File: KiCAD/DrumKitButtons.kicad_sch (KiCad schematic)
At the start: 6 parts, among them J1 Input, J2 Output

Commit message: fix DRC errors
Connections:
- net DI_{LED}: now also J2.4 (Pin_4); no longer J1.4 (Pin_4)
- net DI_{SW}: now also J1.5 (Pin_5); no longer J2.5 (Pin_5)
- net DO_{LED}: now also J1.4 (Pin_4); no longer J2.4 (Pin_4)
- net DO_{SW}: now also J2.5 (Pin_5); no longer J1.5 (Pin_5)
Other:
- moved on the sheet: J1

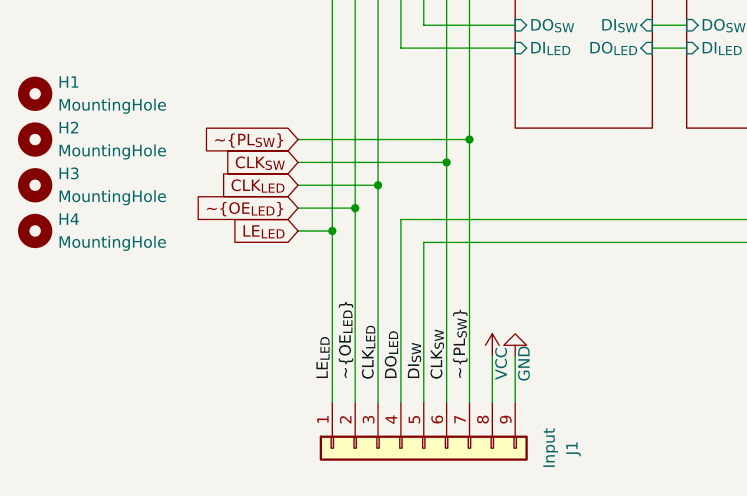
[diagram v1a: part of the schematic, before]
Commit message: reorder buttons/leds
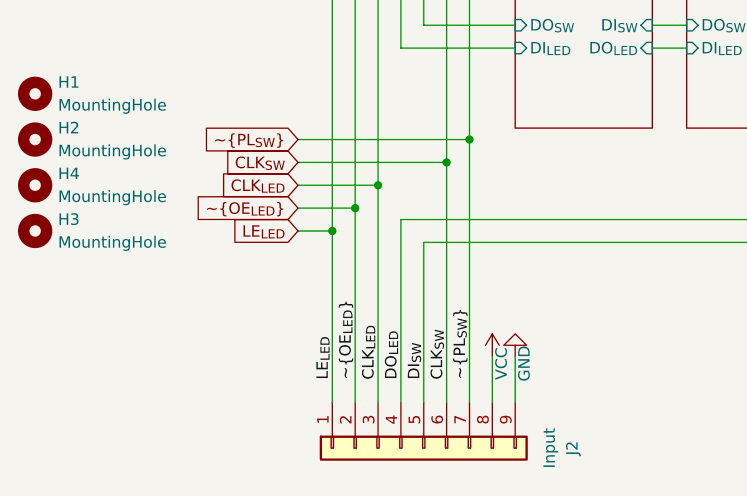
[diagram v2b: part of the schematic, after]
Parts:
- renumbered H4 to H3, H3 to H4, J2 to J1, J1 to J2
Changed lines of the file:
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@@
 		(dnp no)
 		(fields_autoplaced yes)
-		(property "Reference" "J2"
+		(property "Reference" "J1"
 			(at 109.22 46.99 0)
 			(effects
@@
 			(project "DrumKitButtons"
 				(path "/9053e4fd-2214-4e2c-a1c2-d5a9964413b7"
-					(reference "J2")
+					(reference "J1")
 					(unit 1)
 				)
@@
 		(on_board yes)
 		(dnp no)
-		(property "Reference" "#PWR023"
+		(property "Reference" "#PWR04"
 			(at 101.6 119.38 0)
 			(effects
@@
 			(project "DrumKitButtons"
 				(path "/9053e4fd-2214-4e2c-a1c2-d5a9964413b7"
-					(reference "#PWR023")
+					(reference "#PWR04")
 					(unit 1)
 				)
@@
 		(dnp no)
 		(fields_autoplaced yes)
-		(property "Reference" "J1"
+		(property "Reference" "J2"
 			(at 107.95 135.89 0)
 			(effects
@@
 			(project ""
 				(path "/9053e4fd-2214-4e2c-a1c2-d5a9964413b7"
-					(reference "J1")
+					(reference "J2")
 					(unit 1)
 				)
@@
 		(on_board yes)
 		(dnp no)
-		(property "Reference" "#PWR024"
+		(property "Reference" "#PWR03"
 			(at 99.06 129.54 0)
 			(effects
@@
 			(project "DrumKitButtons"
 				(path "/9053e4fd-2214-4e2c-a1c2-d5a9964413b7"
-					(reference "#PWR024")
+					(reference "#PWR03")
 					(unit 1)
 				)
@@
 		(on_board yes)
 		(dnp no)
-		(property "Reference" "#PWR021"
+		(property "Reference" "#PWR01"
 			(at 99.06 55.88 0)
 			(effects
@@
 			(project "DrumKitButtons"
 				(path "/9053e4fd-2214-4e2c-a1c2-d5a9964413b7"
-					(reference "#PWR021")
+					(reference "#PWR01")
 					(unit 1)
 				)
@@
 		(dnp no)
 		(fields_autoplaced yes)
-		(property "Reference" "H4"
+		(property "Reference" "H3"
 			(at 50.8 110.4899 0)
 			(effects
@@
 			(project ""
 				(path "/9053e4fd-2214-4e2c-a1c2-d5a9964413b7"
-					(reference "H4")
+					(reference "H3")
 					(unit 1)
 				)
@@
 		(dnp no)
 		(fields_autoplaced yes)
-		(property "Reference" "H3"
+		(property "Reference" "H4"
 			(at 50.8 105.4099 0)
 			(effects
@@
 			(project ""
 				(path "/9053e4fd-2214-4e2c-a1c2-d5a9964413b7"
-					(reference "H3")
+					(reference "H4")
 					(unit 1)
 				)
@@
 		(on_board yes)
 		(dnp no)
-		(property "Reference" "#PWR022"
+		(property "Reference" "#PWR02"
 			(at 101.6 66.04 0)
 			(effects
@@
 			(project "DrumKitButtons"
 				(path "/9053e4fd-2214-4e2c-a1c2-d5a9964413b7"
-					(reference "#PWR022")
-					(unit 1)
-				)
+					(reference "#PWR02")
+					(unit 1)
+				)

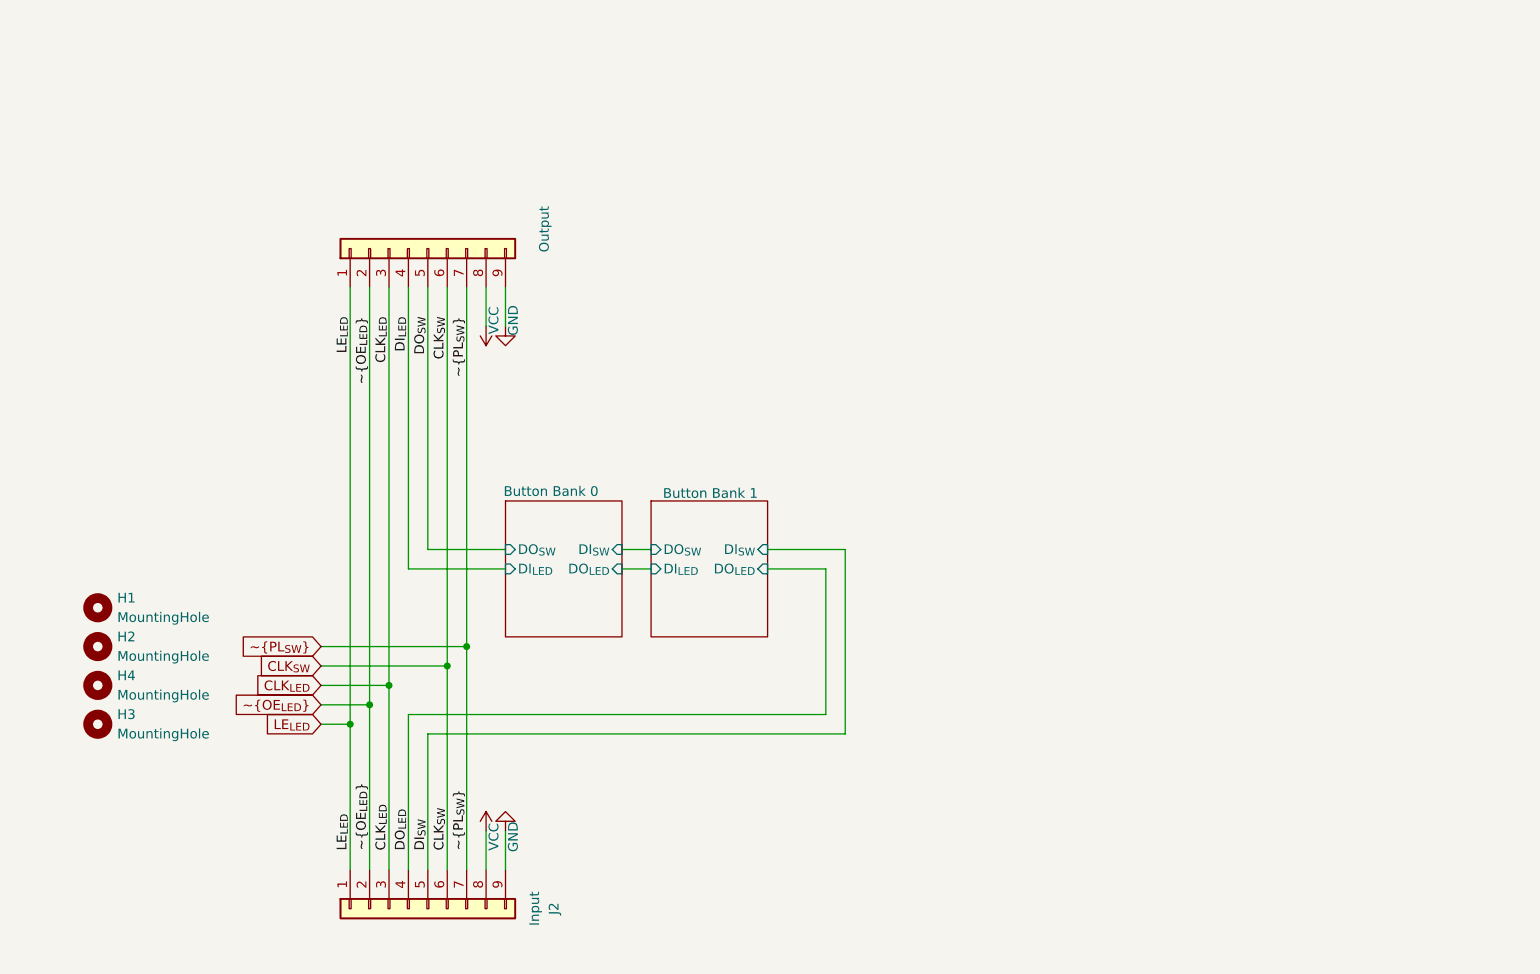
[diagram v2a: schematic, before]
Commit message: make 3 rows in schema; break single button out to its own kicad_sch
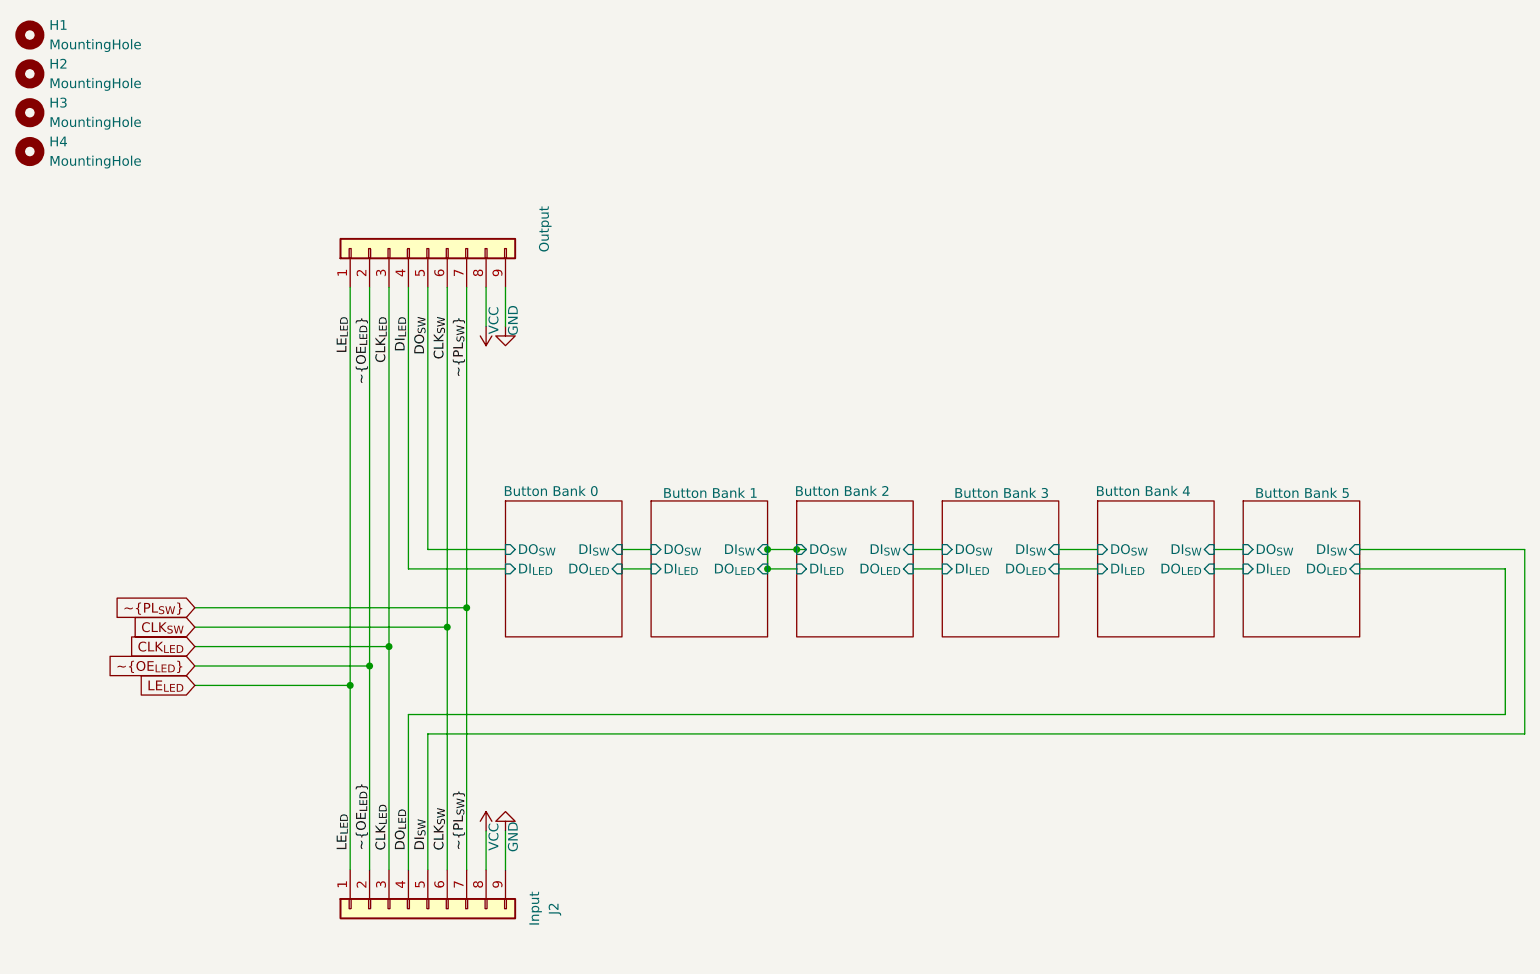
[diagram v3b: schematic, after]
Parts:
- renumbered H4 to H3, H3 to H4
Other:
- added sheet Button Bank 2 (8-buttons.kicad_sch)
- added sheet Button Bank 3 (8-buttons.kicad_sch)
- added sheet Button Bank 4 (8-buttons.kicad_sch)
- added sheet Button Bank 5 (8-buttons.kicad_sch)
- moved on the sheet: H1, H2, H3, H4

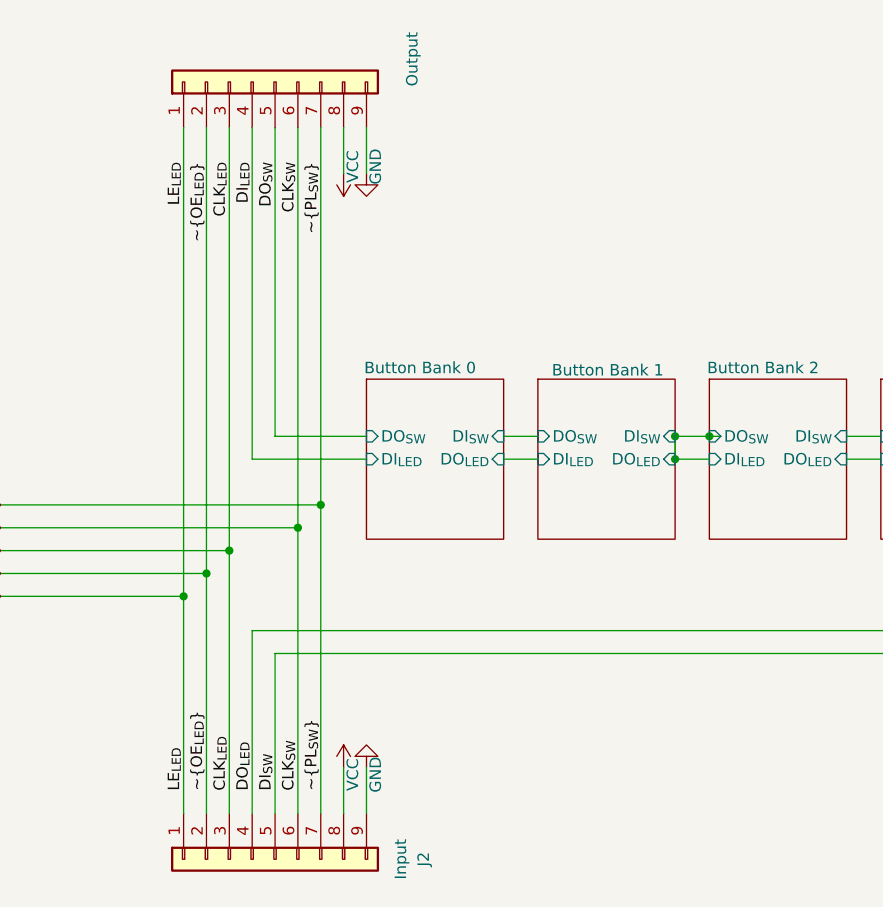
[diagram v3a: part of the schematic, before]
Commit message: 3 rows of 16 buttons; SMT
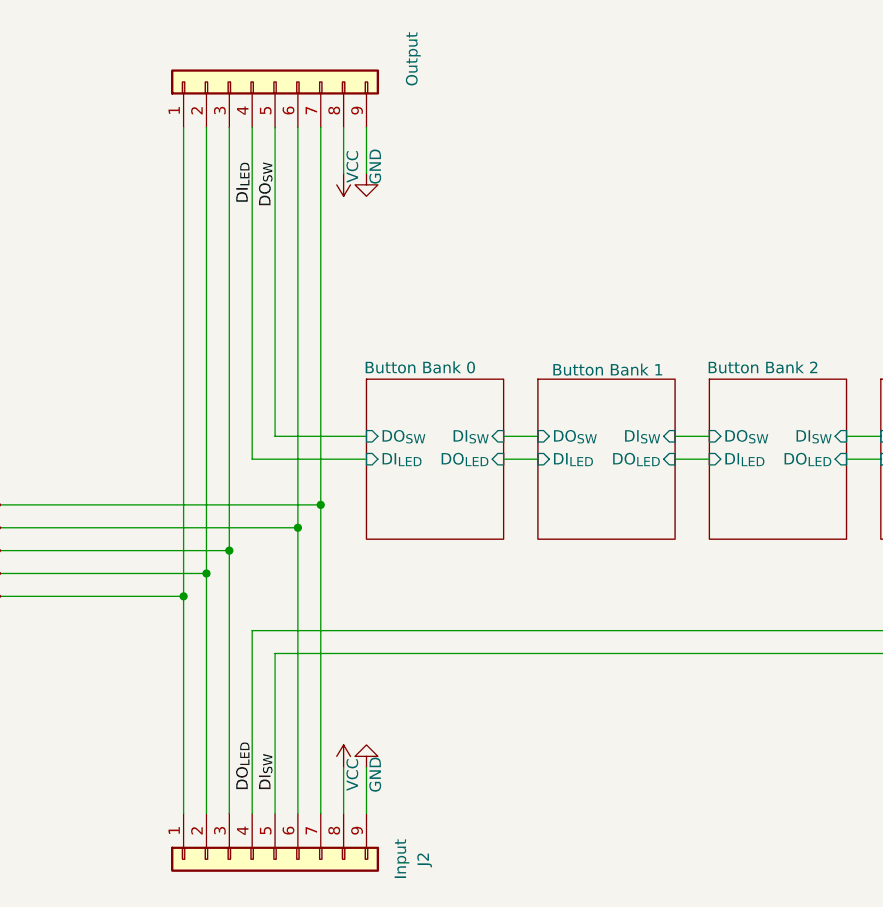
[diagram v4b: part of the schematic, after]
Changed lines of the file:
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@@
-	)
-	(junction
-		(at 135.89 88.9)
-		(diameter 0)
-		(color 0 0 0 0)
-	)
-	(junction
-		(at 139.7 88.9)
-		(diameter 0)
-		(color 0 0 0 0)
-	)
-	(junction
-		(at 135.89 91.44)
-		(diameter 0)
-		(color 0 0 0 0)
 	)
 	(junction
@@
 		(pts
 			(xy 86.36 54.61) (xy 86.36 101.6)
-		)
-		(stroke
-			(width 0)
-			(type default)
-		)
-	)
-	(wire
-		(pts
-			(xy 135.89 88.9) (xy 135.89 91.44)
-		)
-		(stroke
-			(width 0)
-			(type default)
-		)
-	)
-	(wire
-		(pts
-			(xy 139.7 88.9) (xy 140.97 88.9)
 		)
 		(stroke
@@
 		)
 	)
-	(label "LE_{LED}"
-		(at 81.28 128.27 90)
-		(effects
-			(font
-				(size 1.27 1.27)
-			)
-			(justify left bottom)
-		)
-	)
-	(label "~{OE_{LED}}"
-		(at 83.82 58.42 270)
-		(effects
-			(font
-				(size 1.27 1.27)
-			)
-			(justify right bottom)
-		)
-	)
-	(label "CLK_{SW}"
-		(at 93.98 58.42 270)
-		(effects
-			(font
-				(size 1.27 1.27)
-			)
-			(justify right bottom)
-		)
-	)
 	(label "DI_{LED}"
 		(at 88.9 58.42 270)
@@
 		(effects
 			(font
-				(size 1.27 1.27)
-			)
-			(justify left bottom)
-		)
-	)
-	(label "LE_{LED}"
-		(at 81.28 58.42 270)
-		(effects
-			(font
-				(size 1.27 1.27)
-			)
-			(justify right bottom)
-		)
-	)
-	(label "~{OE_{LED}}"
-		(at 83.82 128.27 90)
-		(effects
-			(font
-				(size 1.27 1.27)
-			)
-			(justify left bottom)
-		)
-	)
-	(label "CLK_{LED}"
-		(at 86.36 128.27 90)
-		(effects
-			(font
-				(size 1.27 1.27)
-			)
-			(justify left bottom)
-		)
-	)
-	(label "~{PL_{SW}}"
-		(at 96.52 128.27 90)
-		(effects
-			(font
-				(size 1.27 1.27)
-			)
-			(justify left bottom)
-		)
-	)
-	(label "CLK_{LED}"
-		(at 86.36 58.42 270)
-		(effects
-			(font
-				(size 1.27 1.27)
-			)
-			(justify right bottom)
-		)
-	)
-	(label "~{PL_{SW}}"
-		(at 96.52 58.42 270)
-		(effects
-			(font
-				(size 1.27 1.27)
-			)
-			(justify right bottom)
-		)
-	)
-	(label "CLK_{SW}"
-		(at 93.98 128.27 90)
-		(effects
-			(font

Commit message: Revert "3 rows of 16 buttons; SMT"
This reverts commit c08e4dc0c350e57a2ca7329c2459be699e742724.
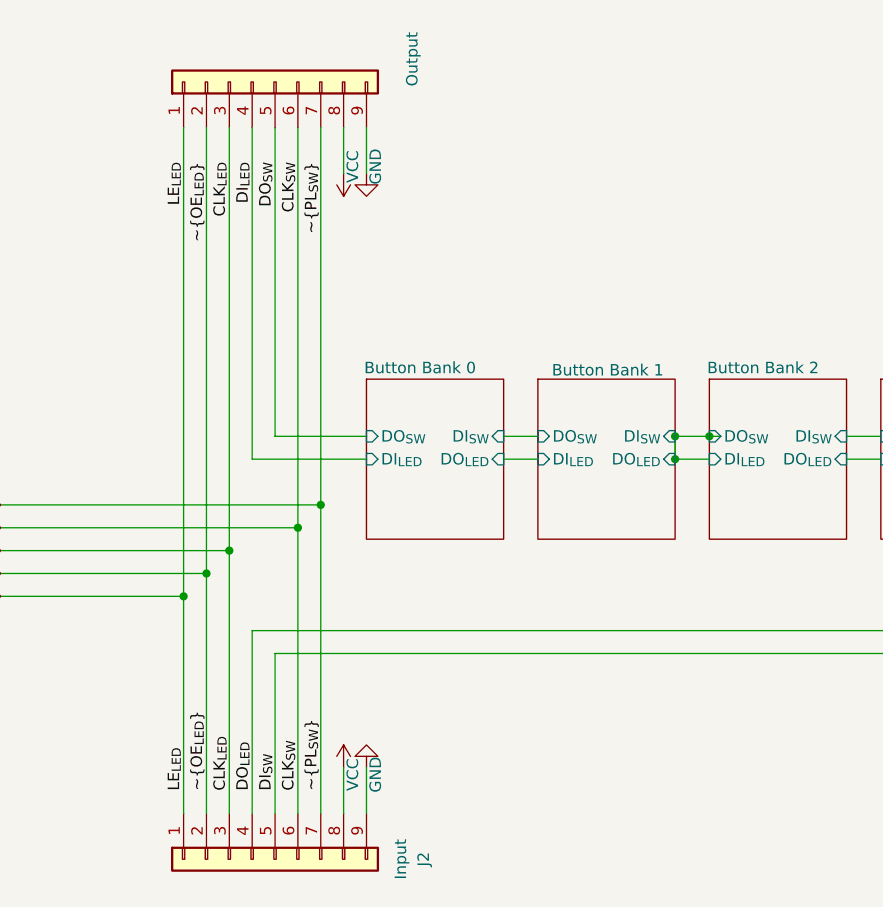
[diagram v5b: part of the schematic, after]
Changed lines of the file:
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@@
+	)
+	(junction
+		(at 135.89 88.9)
+		(diameter 0)
+		(color 0 0 0 0)
+	)
+	(junction
+		(at 139.7 88.9)
+		(diameter 0)
+		(color 0 0 0 0)
+	)
+	(junction
+		(at 135.89 91.44)
+		(diameter 0)
+		(color 0 0 0 0)
 	)
 	(junction
@@
 	(wire
 		(pts
+			(xy 135.89 88.9) (xy 135.89 91.44)
+		)
+		(stroke
+			(width 0)
+			(type default)
+		)
+	)
+	(wire
+		(pts
+			(xy 139.7 88.9) (xy 140.97 88.9)
+		)
+		(stroke
+			(width 0)
+			(type default)
+		)
+	)
+	(wire
+		(pts
 			(xy 93.98 54.61) (xy 93.98 99.06)
 		)
@@
 		)
 	)
+	(label "LE_{LED}"
+		(at 81.28 128.27 90)
+		(effects
+			(font
+				(size 1.27 1.27)
+			)
+			(justify left bottom)
+		)
+	)
+	(label "~{OE_{LED}}"
+		(at 83.82 58.42 270)
+		(effects
+			(font
+				(size 1.27 1.27)
+			)
+			(justify right bottom)
+		)
+	)
+	(label "CLK_{SW}"
+		(at 93.98 58.42 270)
+		(effects
+			(font
+				(size 1.27 1.27)
+			)
+			(justify right bottom)
+		)
+	)
 	(label "DI_{LED}"
 		(at 88.9 58.42 270)
@@
 		(effects
 			(font
+				(size 1.27 1.27)
+			)
+			(justify left bottom)
+		)
+	)
+	(label "LE_{LED}"
+		(at 81.28 58.42 270)
+		(effects
+			(font
+				(size 1.27 1.27)
+			)
+			(justify right bottom)
+		)
+	)
+	(label "~{OE_{LED}}"
+		(at 83.82 128.27 90)
+		(effects
+			(font
+				(size 1.27 1.27)
+			)
+			(justify left bottom)
+		)
+	)
+	(label "CLK_{LED}"
+		(at 86.36 128.27 90)
+		(effects
+			(font
+				(size 1.27 1.27)
+			)
+			(justify left bottom)
+		)
+	)
+	(label "~{PL_{SW}}"
+		(at 96.52 128.27 90)
+		(effects
+			(font
+				(size 1.27 1.27)
+			)
+			(justify left bottom)
+		)
+	)
+	(label "CLK_{LED}"
+		(at 86.36 58.42 270)
+		(effects
+			(font
+				(size 1.27 1.27)
+			)
+			(justify right bottom)
+		)
+	)
+	(label "~{PL_{SW}}"
+		(at 96.52 58.42 270)
+		(effects
+			(font
+				(size 1.27 1.27)
+			)
+			(justify right bottom)
+		)
+	)
+	(label "CLK_{SW}"
+		(at 93.98 128.27 90)
+		(effects
+			(font
